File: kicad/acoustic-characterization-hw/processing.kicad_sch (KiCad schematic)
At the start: 14 parts, among them IC1 ECP5-BGA256, J2 Conn_01x04_Socket

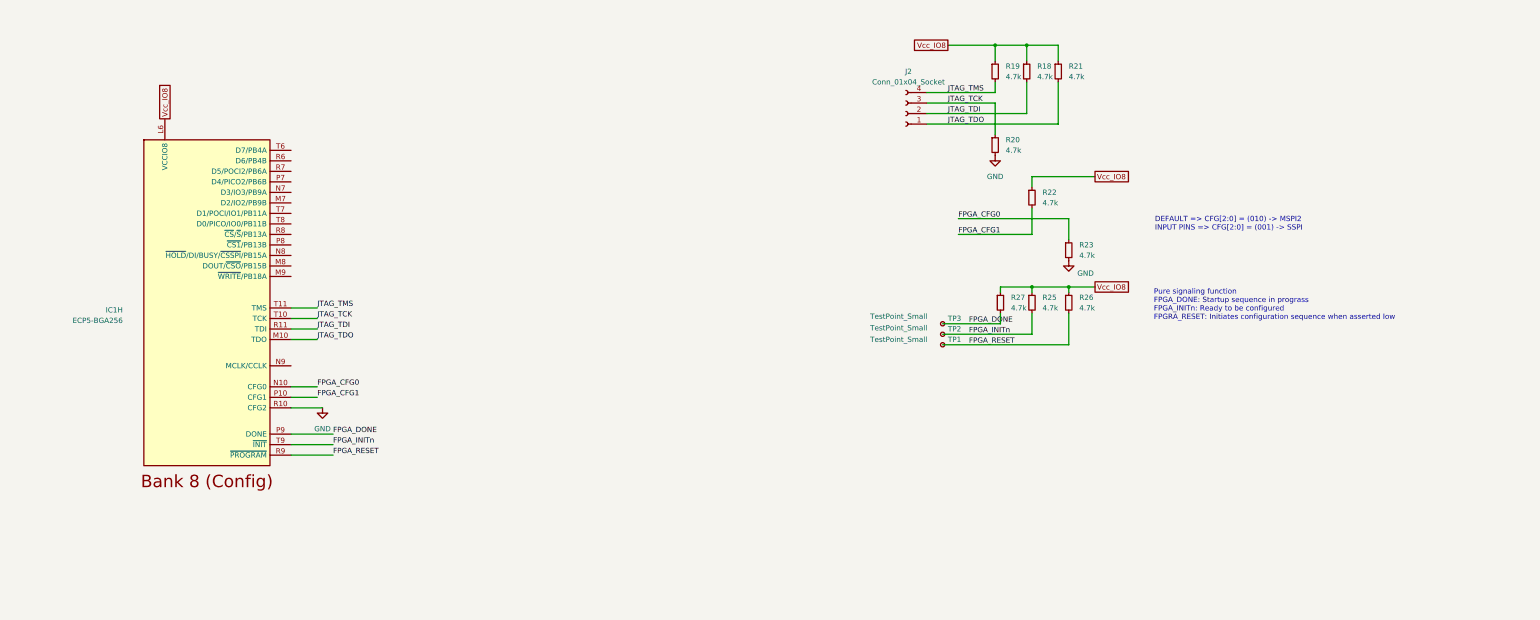
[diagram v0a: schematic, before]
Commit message: [kicad] Added flash memory + flash connection (next) Add RAM and ethernet
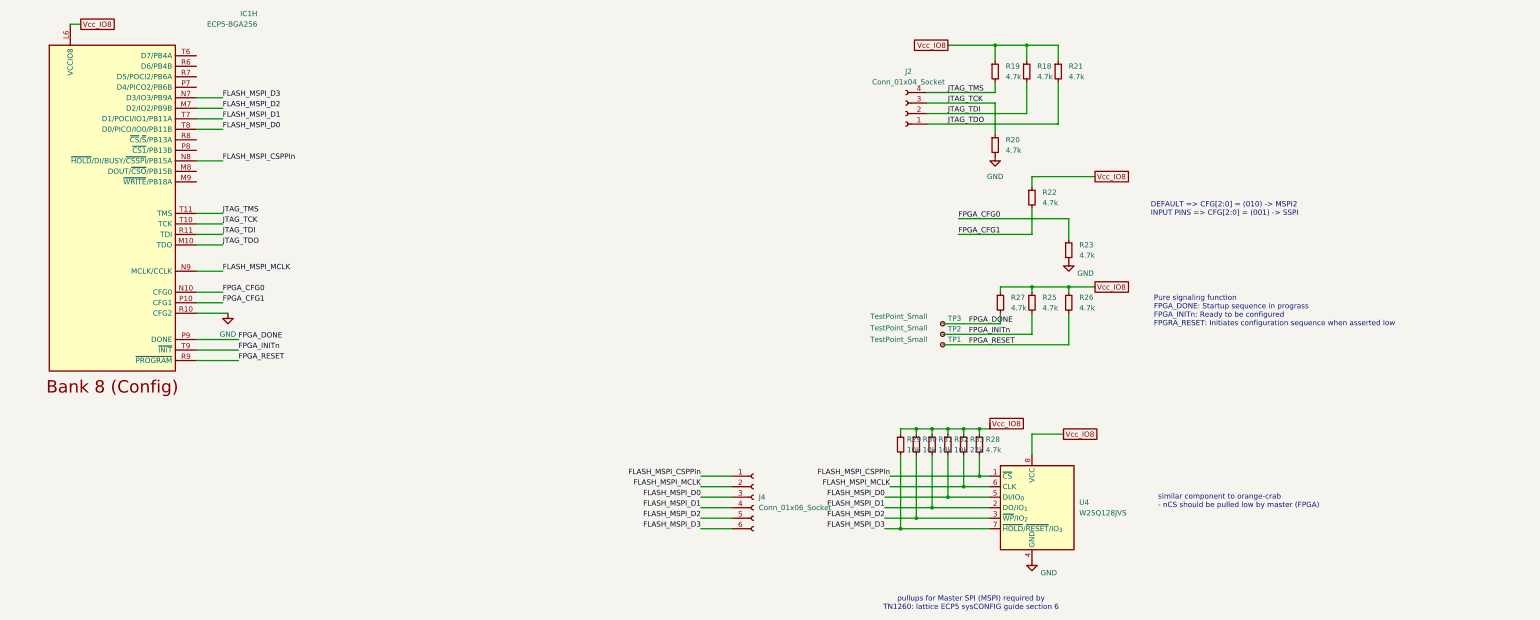
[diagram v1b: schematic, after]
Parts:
- added J4: Conn_01x06_Socket, symbol Connector:Conn_01x06_Socket
- added R28: 4.7k, Resistor_SMD:R_0402_1005Metric, symbol Device:R_Small
- added R29, R30, R31, R32: 10k, Resistor_SMD:R_0402_1005Metric, symbol Device:R_Small
- added R33: 22k, Resistor_SMD:R_0402_1005Metric, symbol Device:R_Small
- added U4: W25Q128JVS, Package_SO:SOIC-8_5.3x5.3mm_P1.27mm, symbol Memory_Flash:W25Q128JVS
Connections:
- net GND: now also U4.4 (GND)
- net Vcc_IO8: now also R28.1, R29.1, R30.1, R31.1, R32.1, R33.1, U4.8 (VCC)
- net FLASH_MSPI_D2: now reaches IC1.M7 (D2/IO2/PB9B)
- net FLASH_MSPI_D2: now also J4.5 (Pin_5), R30.2, U4.3 (~{WP}/IO_{2})
- net FLASH_MSPI_D3: now reaches IC1.N7 (D3/IO3/PB9A)
- net FLASH_MSPI_D3: now also J4.6 (Pin_6), R29.2, U4.7 (~{HOLD}/~{RESET}/IO_{3})
- net FLASH_MSPI_CSPPIn: now reaches IC1.N8 (~{HOLD}/DI/BUSY/~{CSSPI}/PB15A)
- net FLASH_MSPI_CSPPIn: now also J4.1 (Pin_1), R28.2, U4.1 (~{CS})
- net FLASH_MSPI_MCLK: now reaches IC1.N9 (MCLK/CCLK)
- net FLASH_MSPI_MCLK: now also J4.2 (Pin_2), R33.2, U4.6 (CLK)
- net FLASH_MSPI_D1: now reaches IC1.T7 (D1/POCI/IO1/PB11A)
- net FLASH_MSPI_D1: now also J4.4 (Pin_4), R31.2, U4.2 (DO/IO_{1})
- net FLASH_MSPI_D0: now reaches IC1.T8 (D0/PICO/IO0/PB11B)
- net FLASH_MSPI_D0: now also J4.3 (Pin_3), R32.2, U4.5 (DI/IO_{0})
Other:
- note added: "pullups for Master SPI (MSPI) required by TN1260: lattice ECP5 sysCONFIG guide section 6"
- note added: "similar component to orange-crab - nCS should be pulled low by master (FPGA)"
- moved on the sheet: IC1H

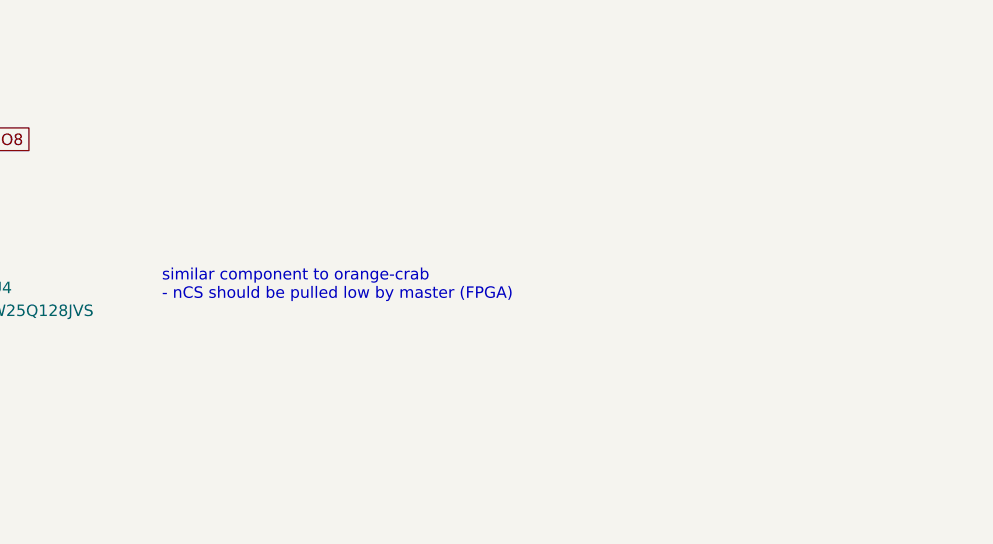
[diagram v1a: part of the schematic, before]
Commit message: [kicad] Chose RAM, connecting pins
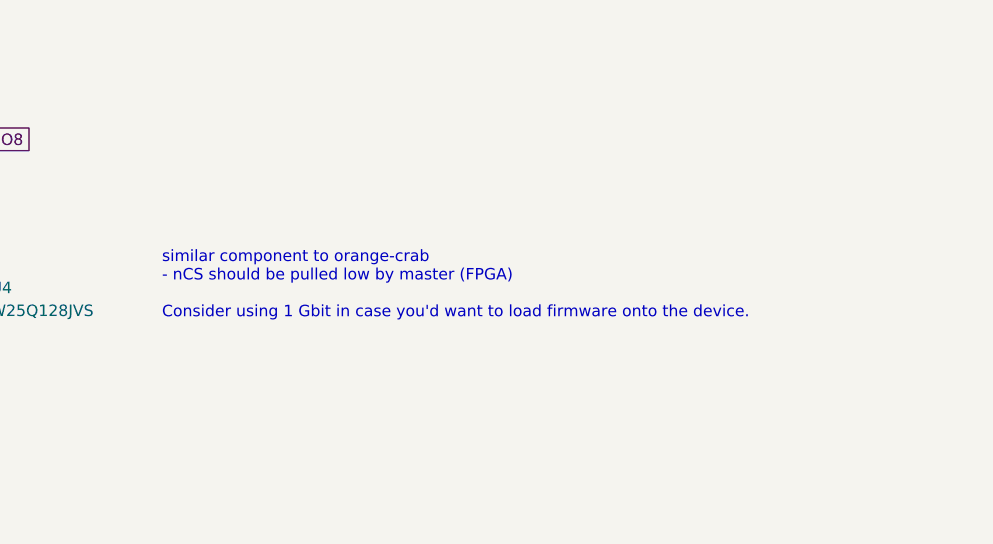
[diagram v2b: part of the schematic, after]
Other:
- note added: "similar component to orange-crab - nCS should be pulled low by master (FPGA) Consider using 1 Gbit in case you'd want to load firmware onto the device."
- note removed: "similar component to orange-crab - nCS should be pulled low by master (FPGA)"
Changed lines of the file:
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@@
 	(generator_version "9.0")
 	(paper "A4")
-	(text "similar component to orange-crab\n- nCS should be pulled low by master (FPGA)"
+	(text "similar component to orange-crab\n- nCS should be pulled low by master (FPGA)\n\nConsider using 1 Gbit in case you'd want to load firmware onto the device."
 		(exclude_from_sim no)
 		(at 289.56 136.906 0)

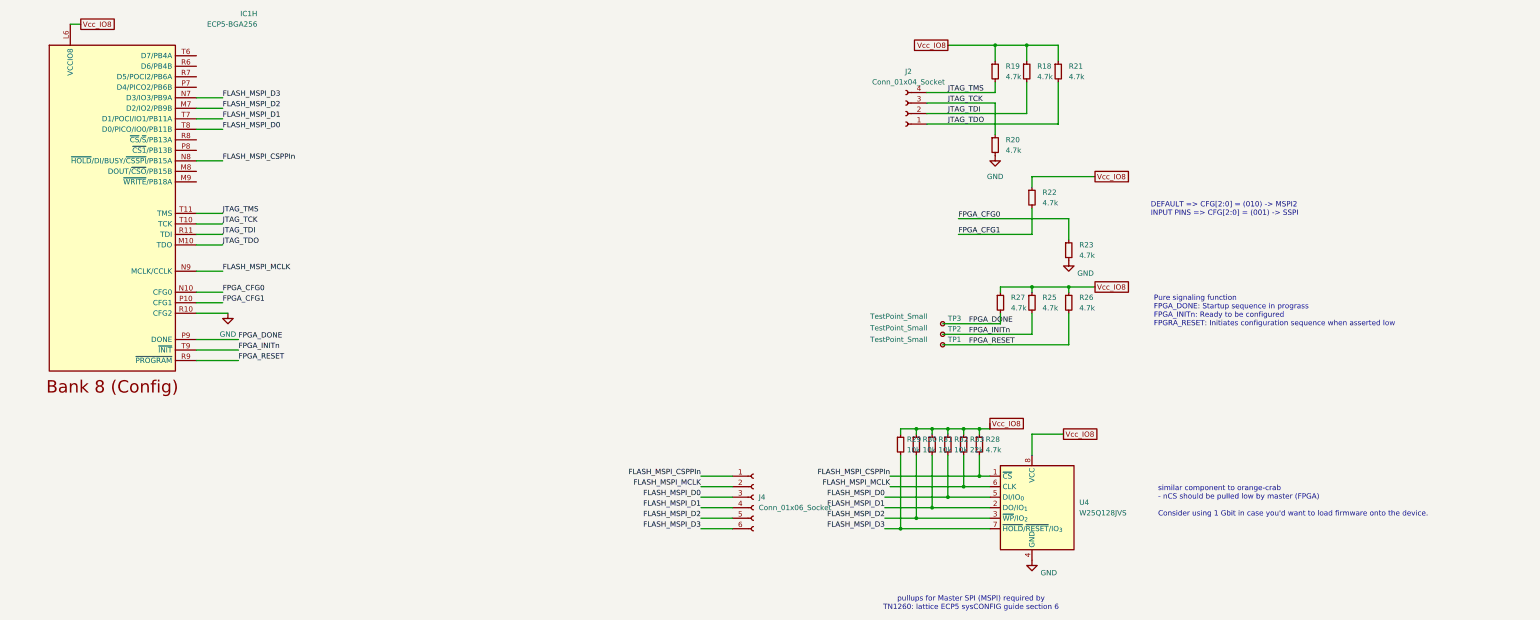
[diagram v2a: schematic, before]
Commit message: [kicad] Connected DDR3L bus, added info on FPGA and ddr pin functionality (next) add filtering circuitry for DDR power pins
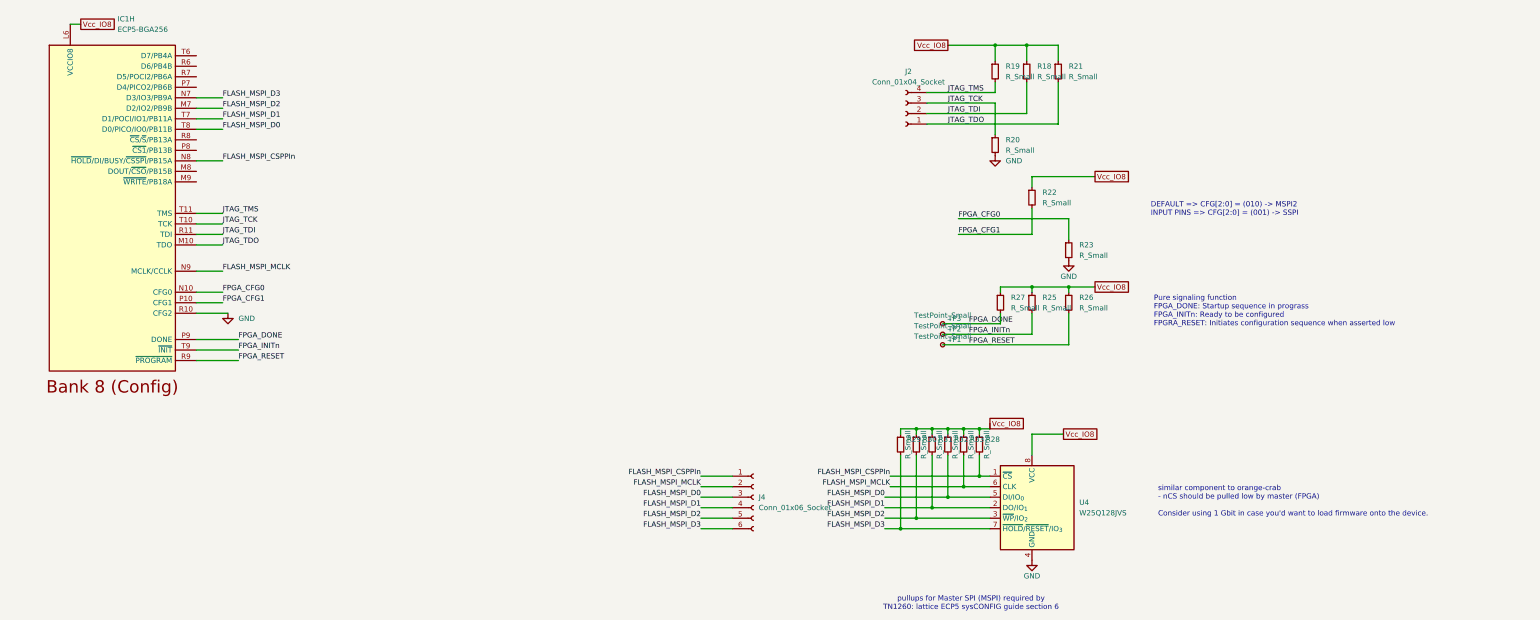
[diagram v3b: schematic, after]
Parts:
- R18, R19, R20, R21, R22, R23, R25, R26, R27, R28: value 4.7k -> R_Small
- R29, R30, R31, R32: value 10k -> R_Small
- R33: value 22k -> R_Small
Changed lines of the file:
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@@
 		(dnp no)
 		(property "Reference" "IC1"
-			(at 71.882 19.05 0)
-			(effects
-				(font
-					(size 1.27 1.27)
-				)
-				(justify right)
+			(at 38.1 20.32 0)
+			(effects
+				(font
+					(size 1.27 1.27)
+				)
+				(justify left)
 			)
 		)
 		(property "Value" "ECP5-BGA256"
-			(at 71.882 21.59 0)
-			(effects
-				(font
-					(size 1.27 1.27)
-				)
-				(justify right)
+			(at 38.1 22.86 0)
+			(effects
+				(font
+					(size 1.27 1.27)
+				)
+				(justify left)
 			)
 		)
@@
 			(project ""
 				(path "/25b015c9-ab13-4427-b72c-b6f348597100/36da1f88-b4f8-4b81-86e1-fac0fb6202fa"
+					(reference "IC1")
+					(unit 8)
+				)
+				(path "/25b015c9-ab13-4427-b72c-b6f348597100/f2b9f5c5-2b83-49a1-9584-962bb926f77f"
 					(reference "IC1")
 					(unit 8)
@@
 		)
 		(property "Value" "GND"
-			(at 272.034 81.788 0)
+			(at 267.97 82.55 0)
 			(effects
 				(font
@@
 		)
 		(property "Value" "TestPoint_Small"
-			(at 219.964 94.996 0)
-			(effects
-				(font
-					(size 1.27 1.27)
-				)
-				(justify left)
+			(at 237.49 94.488 0)
+			(effects
+				(font
+					(size 1.27 1.27)
+				)
 			)
 		)
@@
 		)
 		(property "Value" "TestPoint_Small"
-			(at 219.964 92.202 0)
-			(effects
-				(font
-					(size 1.27 1.27)
-				)
-				(justify left)
+			(at 237.49 91.948 0)
+			(effects
+				(font
+					(size 1.27 1.27)
+				)
 			)
 		)
@@
 			)
 		)
-		(property "Value" "4.7k"
+		(property "Value" "R_Small"
 			(at 261.62 90.1699 0)
 			(effects
@@
 			)
 		)
-		(property "Datasheet" "https://jlcpcb.com/api/file/downloadByFileSystemAccessId/8579705941367193600"
+		(property "Datasheet" "~"
 			(at 259.08 88.9 0)
 			(effects
@@
 			)
 		)
-		(property "Value" "4.7k"
+		(property "Value" "R_Small"
 			(at 270.51 90.1699 0)
 			(effects
@@
 			)
 		)
-		(property "Datasheet" "https://jlcpcb.com/api/file/downloadByFileSystemAccessId/8579705941367193600"
+		(property "Datasheet" "~"
 			(at 267.97 88.9 0)
 			(effects
@@
 		)
 		(property "Value" "GND"
-			(at 64.77 96.52 0)
-			(effects
-				(font
-					(size 1.27 1.27)
-				)
+			(at 67.31 92.7099 0)
+			(effects
+				(font
+					(size 1.27 1.27)
+				)
+				(justify left)
 			)
 		)
@@
 			)
 		)
-		(property "Value" "4.7k"
+		(property "Value" "R_Small"
 			(at 254 90.1699 0)
 			(effects
@@
 			)
 		)
-		(property "Datasheet" "https://jlcpcb.com/api/file/downloadByFileSystemAccessId/8579705941367193600"
+		(property "Datasheet" "~"
 			(at 251.46 88.9 0)
 			(effects
@@
 			)
 		)
-		(property "Value" "4.7k"
+		(property "Value" "R_Small"
 			(at 261.62 64.7699 0)
 			(effects
@@
 			)
 		)
-		(property "Datasheet" "https://jlcpcb.com/api/file/downloadByFileSystemAccessId/8579705941367193600"
+		(property "Datasheet" "~"
 			(at 259.08 63.5 0)
 			(effects
@@
 			)
 		)
-		(property "Value" "10k"
-			(at 236.474 124.46 0)
-			(effects
-				(font
-					(size 1.27 1.27)
-				)
-				(justify left)
+		(property "Value" "R_Small"
+			(at 236.728 123.19 90)
+			(effects
+				(font
+					(size 1.27 1.27)
+				)
 			)
 		)
@@
 			)
 		)
-		(property "Datasheet" "https://jlcpcb.com/api/file/downloadByFileSystemAccessId/8579705941367193600"
+		(property "Datasheet" "~"
 			(at 234.95 123.19 0)
 			(effects
@@
 			)
 		)
-		(property "Value" "4.7k"
-			(at 247.904 124.46 0)
-			(effects
-				(font
-					(size 1.27 1.27)
-				)
-				(justify left)
+		(property "Value" "R_Small"
+			(at 248.158 123.19 90)
+			(effects
+				(font
+					(size 1.27 1.27)
+				)
 			)
 		)
@@
 			)
 		)
-		(property "Datasheet" "https://jlcpcb.com/api/file/downloadByFileSystemAccessId/8579705941367193600"
+		(property "Datasheet" "~"
 			(at 246.38 123.19 0)
 			(effects
@@
 		)
 		(property "Value" "GND"
-			(at 263.144 154.178 0)
+			(at 259.08 154.94 0)
 			(effects
 				(font
@@
 			)
 		)
-		(property "Value" "4.7k"
+		(property "Value" "R_Small"
 			(at 252.73 52.0699 0)
 			(effects
@@
 			)
 		)
-		(property "Datasheet" "https://jlcpcb.com/api/file/downloadByFileSystemAccessId/8579705941367193600"
+		(property "Datasheet" "~"
 			(at 250.19 50.8 0)
 			(effects
@@
 			)
 		)
-		(property "Value" "4.7k"
+		(property "Value" "R_Small"
 			(at 260.35 34.2899 0)
 			(effects
@@
 			)
 		)
-		(property "Datasheet" "https://jlcpcb.com/api/file/downloadByFileSystemAccessId/8579705941367193600"
+		(property "Datasheet" "~"
 			(at 257.81 33.02 0)
 			(effects
@@
 			)
 		)
-		(property "Value" "10k"
-			(at 232.664 124.46 0)
-			(effects
-				(font
-					(size 1.27 1.27)
-				)
-				(justify left)
+		(property "Value" "R_Small"
+			(at 232.918 123.19 90)
+			(effects
+				(font
+					(size 1.27 1.27)
+				)
 			)
 		)
@@
 			)
 		)
-		(property "Datasheet" "https://jlcpcb.com/api/file/downloadByFileSystemAccessId/8579705941367193600"
+		(property "Datasheet" "~"
 			(at 231.14 123.19 0)
 			(effects
@@
 			)
 		)
-		(property "Value" "22k"
-			(at 244.094 124.46 0)
-			(effects
-				(font
-					(size 1.27 1.27)
-				)
-				(justify left)
+		(property "Value" "R_Small"
+			(at 244.348 123.19 90)
+			(effects
+				(font
+					(size 1.27 1.27)
+				)
 			)
 		)
@@
 			)
 		)
-		(property "Datasheet" "https://jlcpcb.com/api/file/downloadByFileSystemAccessId/8579705997331927040"
+		(property "Datasheet" "~"
 			(at 242.57 123.19 0)
 			(effects
@@
 		)
 		(property "Value" "GND"
-			(at 250.19 58.42 0)
-			(effects
-				(font
-					(size 1.27 1.27)
-				)
+			(at 252.73 54.6099 0)
+			(effects
+				(font
+					(size 1.27 1.27)
+				)
+				(justify left)
 			)
 		)
@@
 			)
 		)
-		(property "Value" "10k"
-			(at 228.854 124.46 0)
-			(effects
-				(font
-					(size 1.27 1.27)
-				)
-				(justify left)
+		(property "Value" "R_Small"
+			(at 229.108 123.19 90)
+			(effects
+				(font
+					(size 1.27 1.27)
+				)
 			)
 		)
@@
 			)
 		)
-		(property "Datasheet" "https://jlcpcb.com/api/file/downloadByFileSystemAccessId/8579705941367193600"
+		(property "Datasheet" "~"
 			(at 227.33 123.19 0)
 			(effects
@@
 			)
 		)
-		(property "Value" "10k"
-			(at 240.284 124.46 0)
-			(effects
-				(font
-					(size 1.27 1.27)
-				)
-				(justify left)
+		(property "Value" "R_Small"
+			(at 240.538 123.19 90)
+			(effects
+				(font
+					(size 1.27 1.27)
+				)
 			)
 		)
@@
 			)
 		)
-		(property "Datasheet" "https://jlcpcb.com/api/file/downloadByFileSystemAccessId/8579705941367193600"
+		(property "Datasheet" "~"
 			(at 238.76 123.19 0)
 			(effects
@@
 			)
 		)
-		(property "Value" "4.7k"
+		(property "Value" "R_Small"
 			(at 267.97 34.2899 0)
 			(effects
@@
 			)
 		)
-		(property "Datasheet" "https://jlcpcb.com/api/file/downloadByFileSystemAccessId/8579705941367193600"
+		(property "Datasheet" "~"
 			(at 265.43 33.02 0)
 			(effects
@@
 			)
 		)
-		(property "Value" "4.7k"
+		(property "Value" "R_Small"
 			(at 252.73 34.2899 0)
 			(effects
@@
 			)
 		)
-		(property "Datasheet" "https://jlcpcb.com/api/file/downloadByFileSystemAccessId/8579705941367193600"
+		(property "Datasheet" "~"
 			(at 250.19 33.02 0)
 			(effects
@@
 			)
 		)
-		(property "Value" "4.7k"
+		(property "Value" "R_Small"
 			(at 270.51 77.4699 0)
 			(effects
@@
 			)
 		)
-		(property "Datasheet" "https://jlcpcb.com/api/file/downloadByFileSystemAccessId/8579705941367193600"
+		(property "Datasheet" "~"
 			(at 267.97 76.2 0)
 			(effects
@@
 		)
 		(property "Value" "TestPoint_Small"
-			(at 219.964 97.79 0)
-			(effects
-				(font
-					(size 1.27 1.27)
-				)
-				(justify left)
-			)
-		)
+			(at 237.49 97.028 0)
+			(effects
+				(font
+					(size 1.27 1.27)
+				)
+			)
+		)
